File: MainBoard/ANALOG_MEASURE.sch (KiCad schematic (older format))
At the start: 13 parts

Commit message: R0.1
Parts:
- removed C?: 33uF, symbol Device:C
- removed D?: D, symbol Device:D
- removed D?: D_Zener, symbol Device:D_Zener
- removed Q?: NMOS, symbol Device:Q_NMOS_DGS
- removed R?: 4.7k, symbol Device:R
- removed R?: 25k, symbol Device:R
- removed R?: 330, symbol Device:R
- removed U? (x4): LMV324, symbol Amplifier_Operational:LMV324
- added C?: 0.1uF, symbol Device:C
- added D?: 1N750, symbol Device:D_Zener
- added R?: 4k7, symbol Device:R
- added R?: 10k, symbol Device:R
- R?: value 330 -> 68
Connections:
- net labels added: +6V
- net labels removed: CLR_CURRENT
- wire segments 61 -> 31
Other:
- note added: "VREF = 3V"
- moved on the sheet: R?, U?

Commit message: Layout Main Board
Layout main PCB
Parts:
- C8: renamed from C?; footprint (none) -> Capacitor_THT:C_Rect_L4.0mm_W2.5mm_P2.50mm
- D2: renamed from D?; footprint (none) -> Diode_THT:D_DO-35_SOD27_P10.16mm_Horizontal; P/N (none) -> 1514-1N750ABKPBFREE-ND
- R11: renamed from R?; footprint (none) -> Resistor_THT:R_Axial_DIN0204_L3.6mm_D1.6mm_P7.62mm_Horizontal
- R12: renamed from R?; value 4k7 -> 15k; footprint (none) -> Resistor_THT:R_Axial_DIN0204_L3.6mm_D1.6mm_P7.62mm_Horizontal
- R13: renamed from R?; value 10k -> 27k; footprint (none) -> Resistor_THT:R_Axial_DIN0204_L3.6mm_D1.6mm_P7.62mm_Horizontal; P/N (none) -> RNMF14FAD27K0CT-ND
- U3: renamed from U?; footprint (none) -> Package_DIP:DIP-14_W7.62mm_LongPads
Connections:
- net CURRENT_MEASURE/CUR_VAL: now also U3.4 (CH3); no longer U3.2 (CH1)
- net LINE_VOLTAGE_MEASURE/LINE_ADC: now also U3.3 (CH2); no longer U3.1 (CH0)
- net VREF: now reaches R12.1, R13.1, U3.13 (Vref)
- net CLK renamed SPI0
- net CS_ADC renamed SPI3
- net DIN renamed SPI2
- net DOUT renamed SPI1
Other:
- note added: "SPI PIN NAMING\n0 - CLK\n1 - MISO\n2 - MOSI\n3 - CS_ADC\n4 - CS_STEP\n5 - CS_SD"
- moved on the sheet: C8, D2, R11, R12, R13, U3

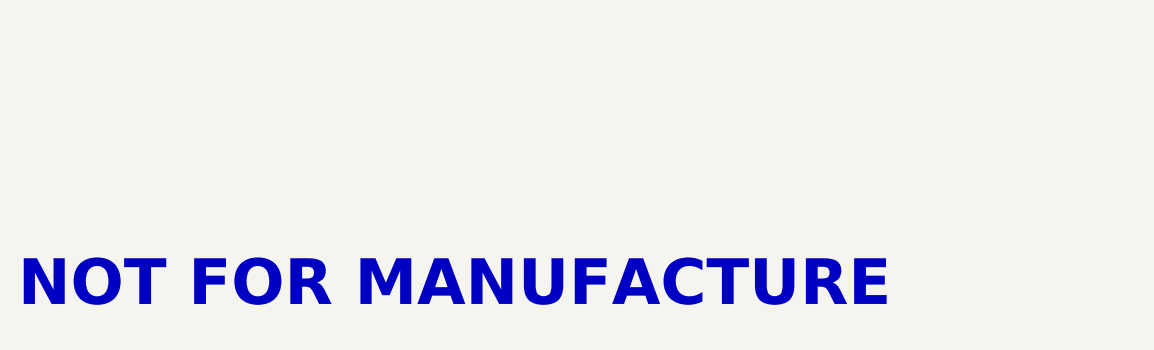
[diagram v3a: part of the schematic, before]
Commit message: Update Voltage Divider
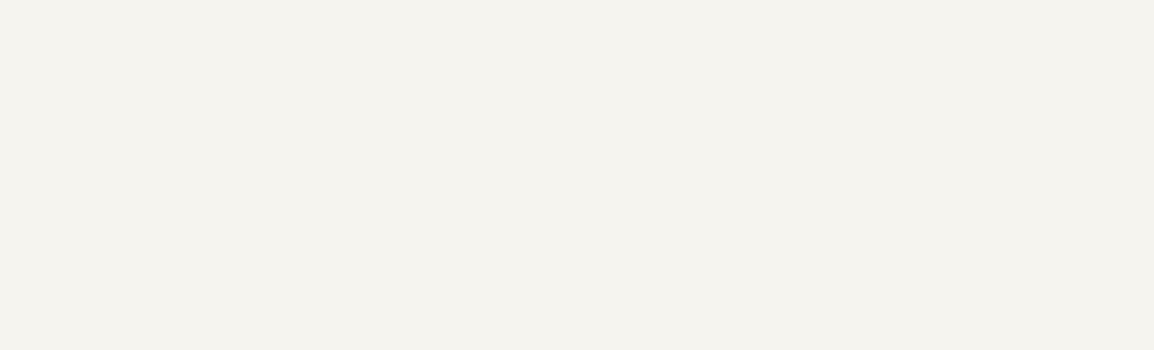
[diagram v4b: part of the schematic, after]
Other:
- note removed: "NOT FOR MANUFACTURE"
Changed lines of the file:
@@
 Sheet 2 5
 Title "PanelIQ Main Board"
-Date "2022-01-31"
-Rev "0.1"
+Date "2022-02-10"
+Rev "A"
 Comp "Drawn By: Thomas Beckley"
 Comment1 "Checked By: "
@@
 Text Label 8250 4200 2    50   ~ 0
 SPI0
-Text Notes 550  7700 0    200  ~ 40
-NOT FOR MANUFACTURE
 Wire Bus Line
 	4250 4750 3950 4750
